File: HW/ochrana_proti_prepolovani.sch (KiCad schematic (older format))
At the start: 2 parts, among them Q7 Q_PMOS_DGS

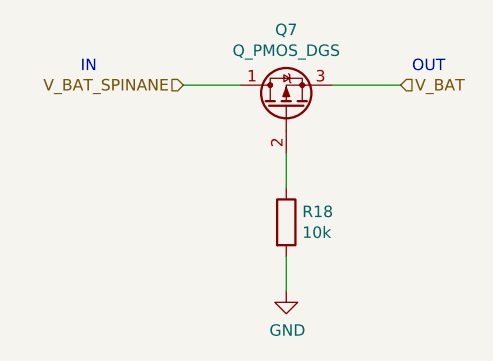
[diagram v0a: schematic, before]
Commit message: repair some misakes from prototype
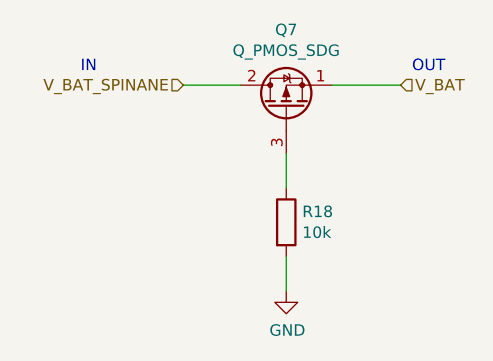
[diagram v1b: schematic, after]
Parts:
- removed Q7: Q_PMOS_DGS, Package_TO_SOT_SMD:SOT-23, symbol Device:Q_PMOS_DGS
- added Q7: Q_PMOS_SDG, symbol Device:Q_PMOS_SDG
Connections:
- net V_BAT: now also Q7.1 (S)
- net V_BAT_SPINANE: now also Q7.2 (D)
- net at R18.1: now also Q7.3 (G)
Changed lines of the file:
@@
 $EndDescr
-$Comp
-L Device:Q_PMOS_DGS Q?
-U 1 1 5F76D204
-P 5450 2550
-AR Path="/5F76D204" Ref="Q?"  Part="1"
-AR Path="/5F7BA54B/5F76D204" Ref="Q?"  Part="1"
-AR Path="/5F7BA54B/5F7BCB45/5F76D204" Ref="Q?"  Part="1"
-AR Path="/5F7BA54B/5F7BCBA6/5F76D204" Ref="Q?"  Part="1"
-AR Path="/5F7BA54B/5F7BCC0A/5F76D204" Ref="Q?"  Part="1"
-AR Path="/5F7BA54B/5F7BCC69/5F76D204" Ref="Q?"  Part="1"
-AR Path="/5F76D05B/5F76D204" Ref="Q7"  Part="1"
-F 0 "Q7" V 5792 2550 50  0000 C CNN
-F 1 "Q_PMOS_DGS" V 5701 2550 50  0000 C CNN
-F 2 "Package_TO_SOT_SMD:SOT-23" H 5650 2650 50  0001 C CNN
-F 3 "~" H 5450 2550 50  0001 C CNN
-F 4 "C15127" H 5450 2550 50  0001 C CNN "LCSC"
-F 5 "0;0;180" H 5450 2550 50  0001 C CNN "JLCPCB_CORRECTION"
-	1    5450 2550
-	0    -1   -1   0
-$EndComp
 $Comp
 L Device:R R?
@@
 	1    0    0    -1
 $EndComp
+$Comp
+L Device:Q_PMOS_SDG Q7
+U 1 1 5FAF5D87
+P 5450 2550
+F 0 "Q7" V 5792 2550 50  0000 C CNN
+F 1 "Q_PMOS_SDG" V 5701 2550 50  0000 C CNN
+F 2 "" H 5650 2650 50  0001 C CNN
+F 3 "~" H 5450 2550 50  0001 C CNN
+	1    5450 2550
+	0    -1   -1   0
+$EndComp
 $EndSCHEMATC

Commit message: start place components
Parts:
- Q3: renamed from Q7; footprint (none) -> Package_TO_SOT_SMD:SOT-23
- renumbered R18 to R13
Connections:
- net V_BAT_SPINANE renamed +5V
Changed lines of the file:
@@
 $Descr A4 11693 8268
 encoding utf-8
-Sheet 11 30
+Sheet 17 29
 Title ""
 Date ""
@@
 AR Path="/5F7BA54B/5F7BCC0A/5F76D20A" Ref="R?"  Part="1"
 AR Path="/5F7BA54B/5F7BCC69/5F76D20A" Ref="R?"  Part="1"
-AR Path="/5F76D05B/5F76D20A" Ref="R18"  Part="1"
-F 0 "R18" H 5520 3096 50  0000 L CNN
+AR Path="/5F76D05B/5F76D20A" Ref="R13"  Part="1"
+F 0 "R13" H 5520 3096 50  0000 L CNN
 F 1 "10k" H 5520 3005 50  0000 L CNN
 F 2 "Resistor_SMD:R_0402_1005Metric" V 5380 3050 50  0001 C CNN
@@
 Wire Wire Line
 	5450 3200 5450 3350
-Text HLabel 5000 2450 0    50   Input ~ 0
-V_BAT_SPINANE
 Text Notes 4550 2400 0    50   ~ 0
 IN\n
@@
 V_BAT
 $Comp
-L power:GND #PWR0314
+L power:GND #PWR0131
 U 1 1 5F76D2C3
 P 5450 3350
-F 0 "#PWR0314" H 5450 3100 50  0001 C CNN
+F 0 "#PWR0131" H 5450 3100 50  0001 C CNN
 F 1 "GND" H 5455 3177 50  0000 C CNN
 F 2 "" H 5450 3350 50  0001 C CNN
@@
 $EndComp
 $Comp
-L Device:Q_PMOS_SDG Q7
+L Device:Q_PMOS_SDG Q3
 U 1 1 5FAF5D87
 P 5450 2550
-F 0 "Q7" V 5792 2550 50  0000 C CNN
+F 0 "Q3" V 5792 2550 50  0000 C CNN
 F 1 "Q_PMOS_SDG" V 5701 2550 50  0000 C CNN
-F 2 "" H 5650 2650 50  0001 C CNN
+F 2 "Package_TO_SOT_SMD:SOT-23" H 5650 2650 50  0001 C CNN
 F 3 "~" H 5450 2550 50  0001 C CNN
 	1    5450 2550
 	0    -1   -1   0
 $EndComp
+$Comp
+L power:+5V #PWR0130
+U 1 1 5FBBB317
+P 5000 2450
+F 0 "#PWR0130" H 5000 2300 50  0001 C CNN
+F 1 "+5V" V 5015 2578 50  0000 L CNN
+F 2 "" H 5000 2450 50  0001 C CNN
+F 3 "" H 5000 2450 50  0001 C CNN
+	1    5000 2450
+	0    -1   -1   0
+$EndComp
